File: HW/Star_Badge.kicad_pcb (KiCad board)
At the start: 2 copper layers, 180 x 171.6 mm, 55 parts, among them J1 AVR-ISP-6, J2 10118194-0001LF, Q1 Q_NMOS_DGS, Q2 Q_PMOS_DGS, U1 ATTINY861-15XD, U2 TPS613221ADBVT, U3 AP7363-33D-13, X1 Badgelife_sao_connector_v169b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, X2 Badgelife_sao_connector_v169b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, X3 Badgelife_sao_connector_v169b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

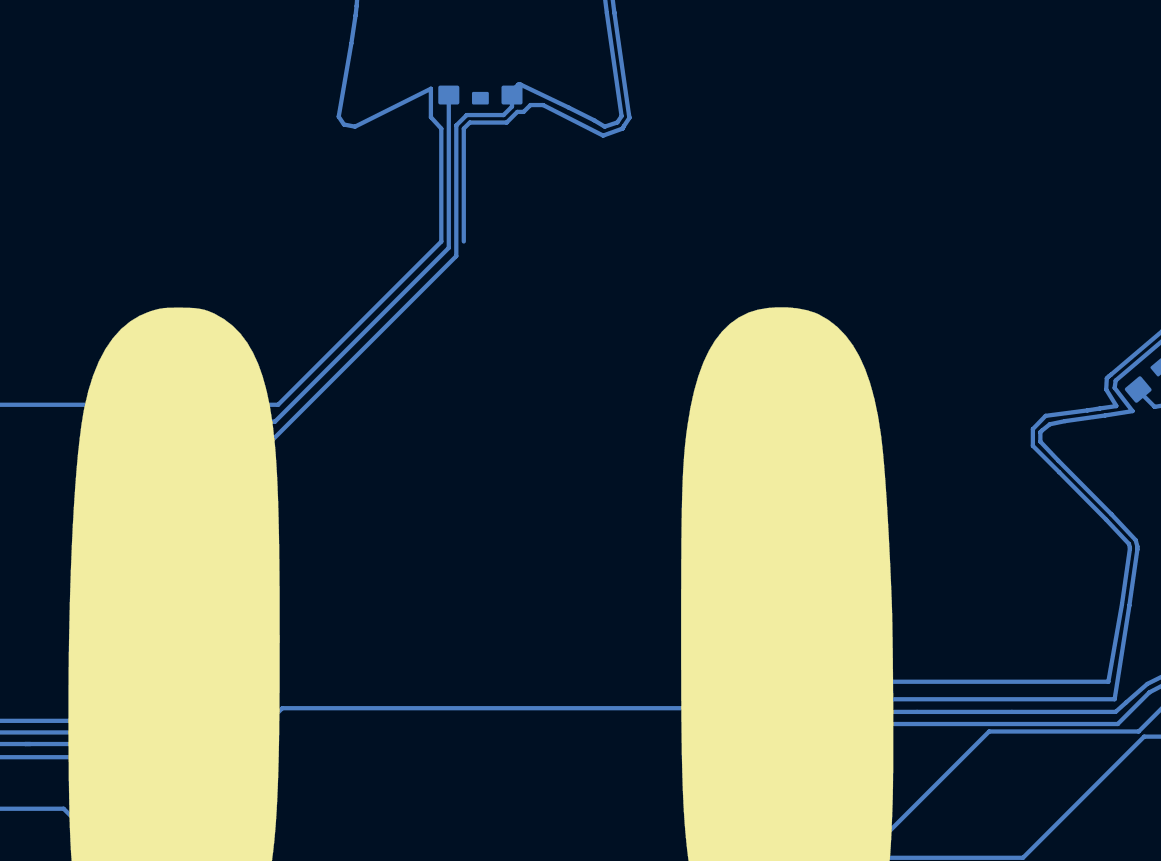
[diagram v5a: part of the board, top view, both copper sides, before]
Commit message: R_LED_BUS connected
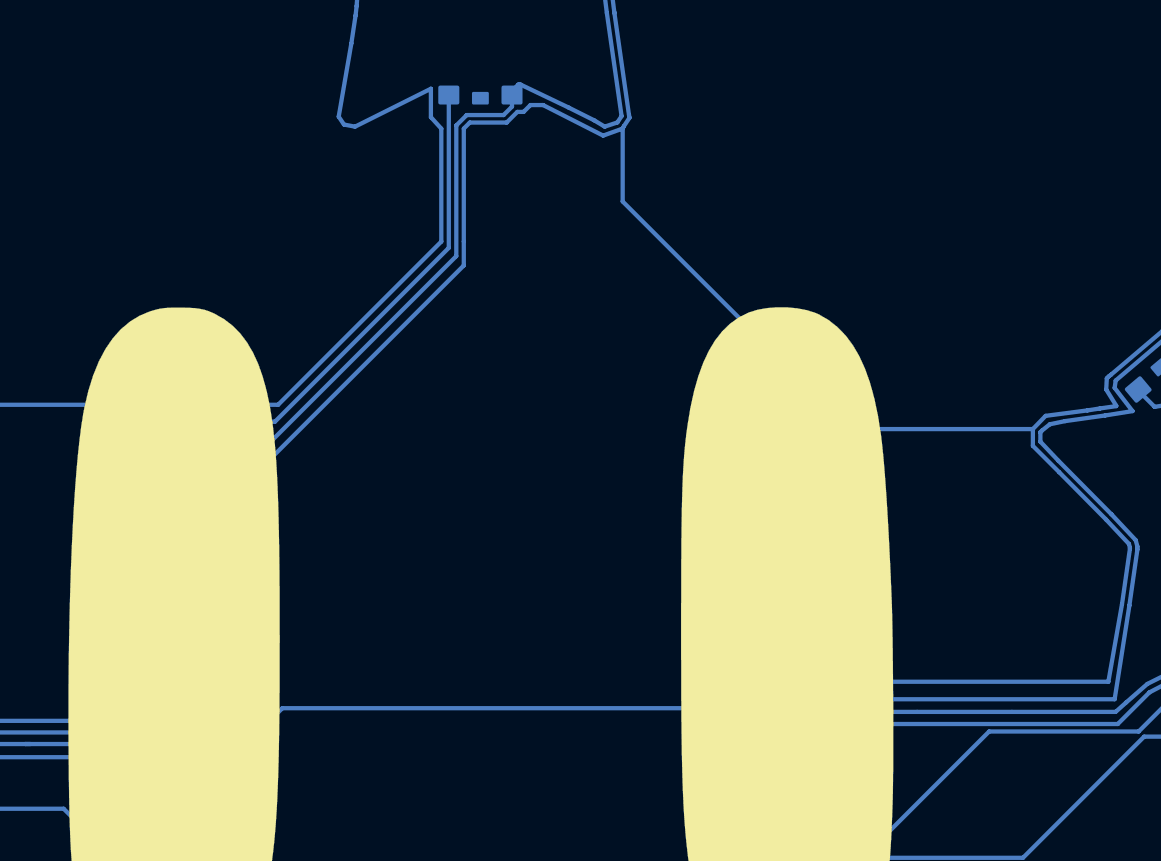
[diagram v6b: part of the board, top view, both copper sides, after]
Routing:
- net /R_LED_BUS: track 223.2 -> 287.0 mm, vias 6 -> 10
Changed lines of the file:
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@@
     (thickness 1.6)
     (drawings 611)
-    (tracks 864)
+    (tracks 885)
     (zones 0)
     (modules 55)
@@
     )
   )
-  (module Star_Badge:F.Silk_g6460 locked (layer F.Cu)
+  (module Star_Badge:F.Silk_g6460 (layer F.Cu)
     (at 100 100)
     (fp_text reference G*** (at 0 0) (layer F.SilkS) hide
@@
   (segment (start 118.274998 113.55) (end 118.3 113.524998) (width 0.2032) (layer F.Cu) (net 6))
   (segment (start 115.875 113.55) (end 118.274998 113.55) (width 0.2032) (layer F.Cu) (net 6))
+  (segment (start 99.21122 80.25) (end 99.21122 81.38878) (width 0.2032) (layer B.Cu) (net 6))
+  (segment (start 99.21122 81.38878) (end 90 90.6) (width 0.2032) (layer B.Cu) (net 6))
+  (segment (start 90 90.6) (end 89.2 90.6) (width 0.2032) (layer B.Cu) (net 6))
+  (segment (start 89.2 90.6) (end 89.2 90.6) (width 0.2032) (layer B.Cu) (net 6))
+  (via (at 89.2 90.6) (size 0.4) (drill 0.3) (layers F.Cu B.Cu) (net 6))
+  (segment (start 89.2 90.6) (end 83.6 90.6) (width 0.2032) (layer F.Cu) (net 6))
+  (segment (start 83.6 90.6) (end 83.4 90.6) (width 0.2032) (layer F.Cu) (net 6))
+  (segment (start 83.4 90.6) (end 83.4 90.6) (width 0.2032) (layer F.Cu) (net 6))
+  (via (at 83.4 90.6) (size 0.4) (drill 0.3) (layers F.Cu B.Cu) (net 6))
+  (segment (start 83.4 103.525) (end 83.375 103.55) (width 0.2032) (layer B.Cu) (net 6))
+  (segment (start 83.4 90.6) (end 83.4 103.525) (width 0.2032) (layer B.Cu) (net 6))
+  (segment (start 126.21939 89.152702) (end 118.647298 89.152702) (width 0.2032) (layer B.Cu) (net 6))
+  (segment (start 118.647298 89.152702) (end 118.647298 89.152702) (width 0.2032) (layer B.Cu) (net 6))
+  (via (at 118.647298 89.152702) (size 0.4) (drill 0.3) (layers F.Cu B.Cu) (net 6))
+  (segment (start 106.752192 74.890782) (end 106.752192 78.352192) (width 0.2032) (layer B.Cu) (net 6))
+  (segment (start 106.752192 78.352192) (end 112.6 84.2) (width 0.2032) (layer B.Cu) (net 6))
+  (segment (start 112.6 84.2) (end 112.6 84.2) (width 0.2032) (layer B.Cu) (net 6))
+  (via (at 112.6 84.2) (size 0.4) (drill 0.3) (layers F.Cu B.Cu) (net 6))
+  (segment (start 118.647298 89.152702) (end 112.952702 89.152702) (width 0.2032) (layer F.Cu) (net 6))
+  (segment (start 112.6 88.8) (end 112.6 84.2) (width 0.2032) (layer F.Cu) (net 6))
+  (segment (start 112.952702 89.152702) (end 112.6 88.8) (width 0.2032) (layer F.Cu) (net 6))
   (segment (start 98.9 56.425887) (end 99.6 55.1) (width 0.2032) (layer B.Cu) (net 11))
   (segment (start 97.4 59.3) (end 98.9 56.425887) (width 0.2032) (layer B.Cu) (net 11))

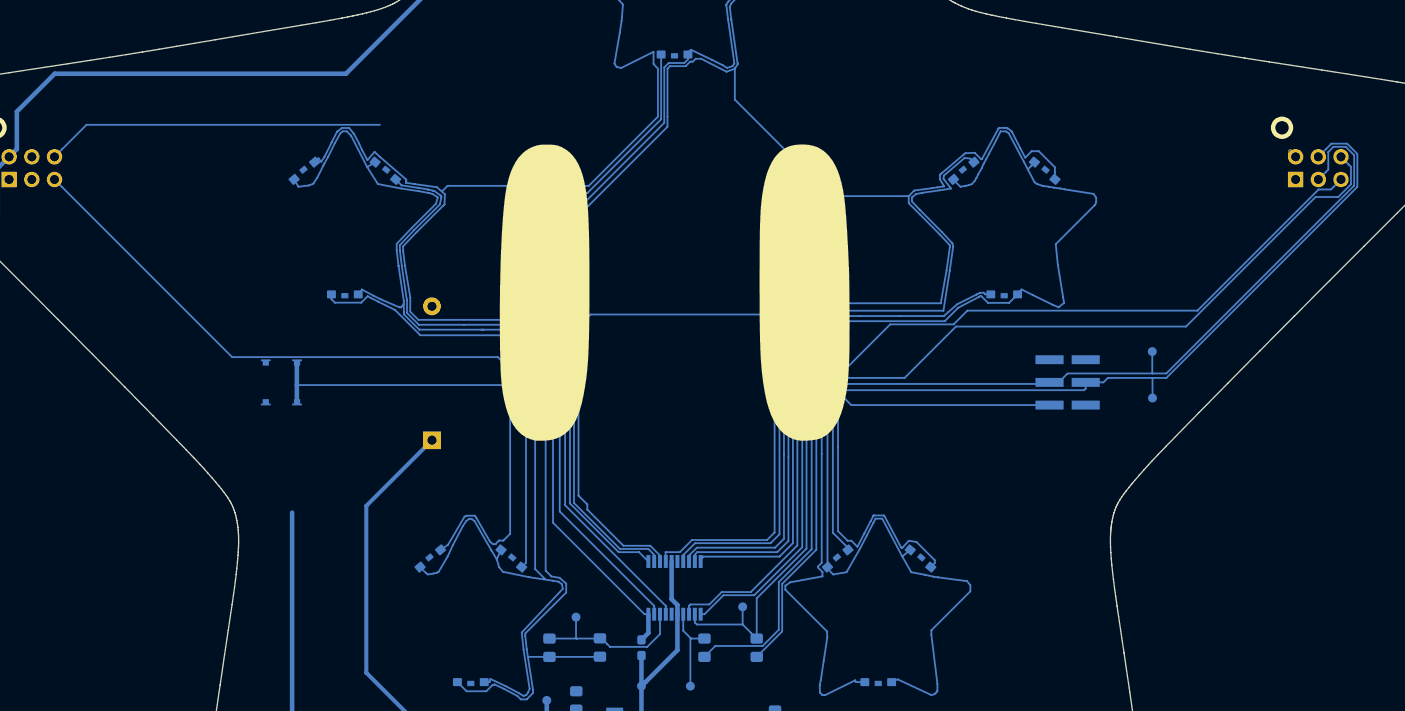
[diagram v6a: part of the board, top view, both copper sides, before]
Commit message: fixed issue with soldermask being pulled around eyes silk
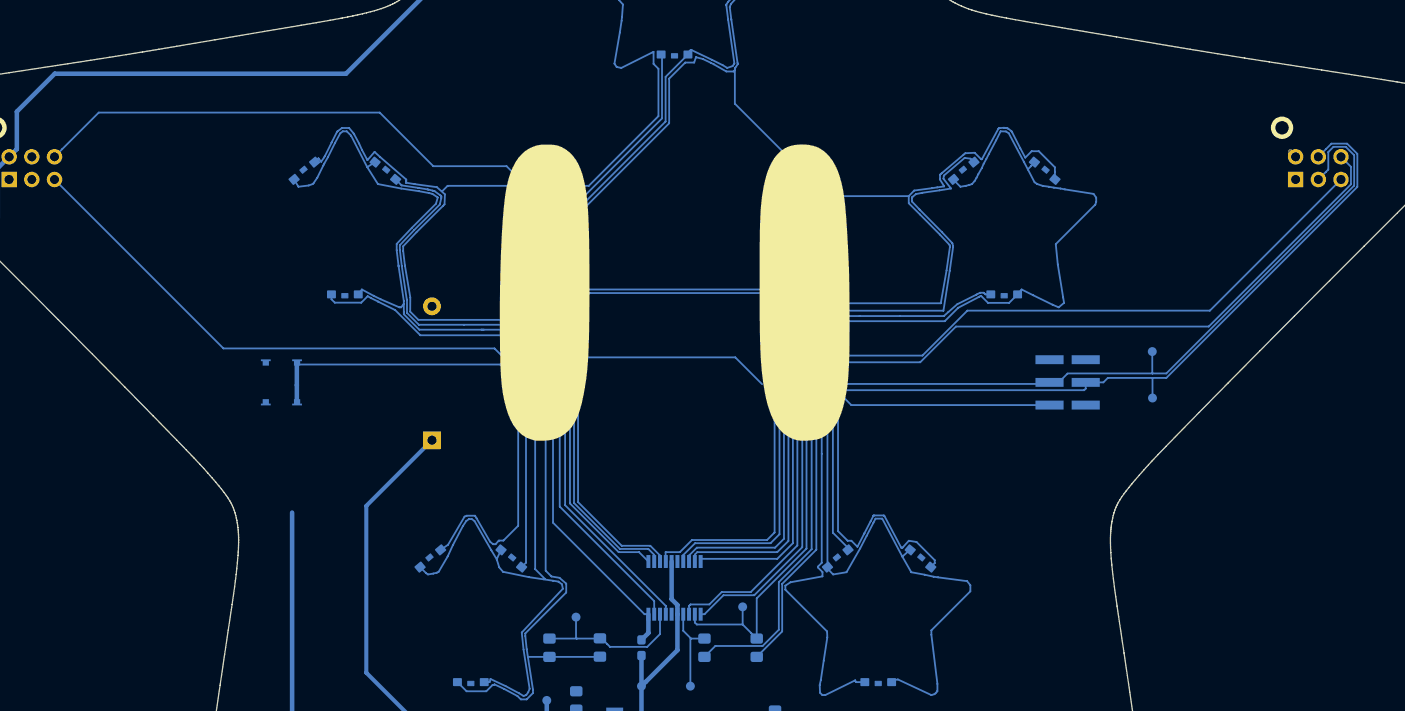
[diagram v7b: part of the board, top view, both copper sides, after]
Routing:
- net /GPIO_2_1: track 69.7 -> 136.7 mm
- net /~RESET: track 36.6 -> 61.3 mm, vias 0 -> 2
- net /B_LED_BUS: track 179.9 -> 199.2 mm, vias 3 -> 2
- net /EN_RGB2: track 97.1 -> 113.8 mm, vias 1 -> 0
- net /EN_RGB3: track 89.3 -> 97.0 mm, vias 0 -> 2
- net /G_LED_BUS: track 286.4 -> 291.1 mm
- net /EN_RGB0: track 103.0 -> 106.6 mm
- net /R_LED_BUS: track 287.0 -> 284.0 mm
- net /GPIO_1_2: track 100.9 -> 102.6 mm
- net /GPIO_1_1: track 103.9 -> 105.5 mm
- net /Button: track 63.7 -> 65.2 mm
